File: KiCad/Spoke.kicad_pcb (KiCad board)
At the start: 2 copper layers, 50 x 100 mm, 128 parts, among them J1 B2B-PH-K-S, J10 BL-A, J11 BL-C, J12 Amphenol 132289, J2 BAT+, J3 BAT-, J4 GCT USB4105/USB4110, J5 CHG+, J6 CHG-, J7 PLS-1x3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

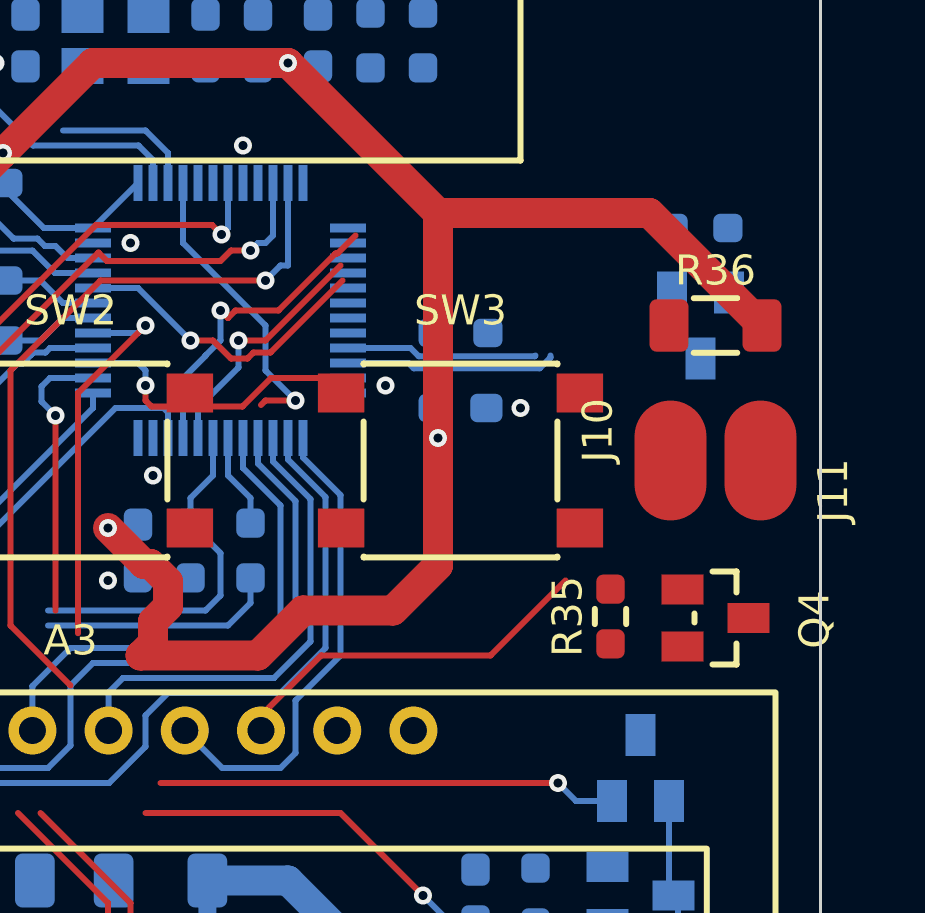
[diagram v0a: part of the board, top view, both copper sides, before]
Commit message: Route BL
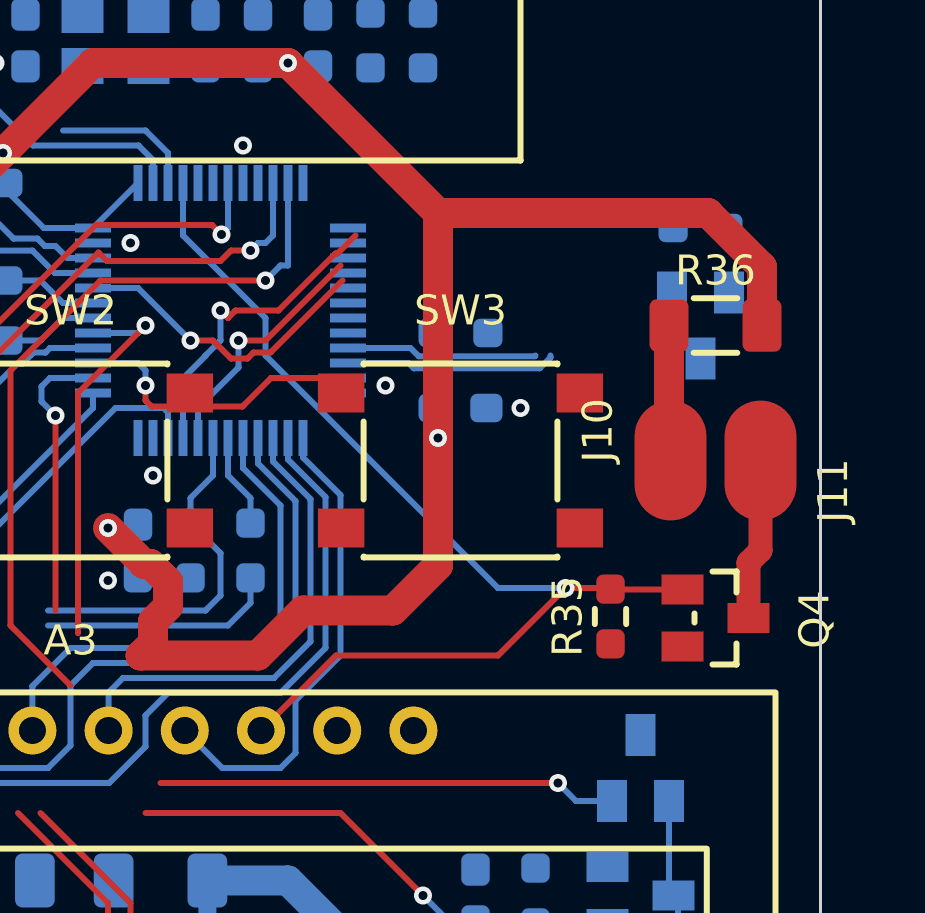
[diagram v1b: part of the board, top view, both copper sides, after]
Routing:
- net LCD_BL: track 22.0 -> 36.1 mm
- net Net-(Q4-D): track 0.00 -> 4.42 mm
- net Net-(J10-Pad1): track 0.00 -> 3.52 mm
- net +3V3: track 275.3 -> 276.4 mm
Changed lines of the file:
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@@
 	)
 	(segment
+		(start 121.25 91.75)
+		(end 123.05 93.55)
+		(width 1)
+		(layer "F.Cu")
+		(net 3)
+	)
+	(segment
 		(start 94.5 114)
 		(end 91.090214 114)
@@
 	)
 	(segment
-		(start 119.3 91.75)
-		(end 123.05 95.5)
-		(width 1)
-		(layer "F.Cu")
-		(net 3)
-	)
-	(segment
 		(start 84.25 72.75)
 		(end 84.75 73.25)
@@
 	)
 	(segment
+		(start 112.25 91.75)
+		(end 121.25 91.75)
+		(width 1)
+		(layer "F.Cu")
+		(net 3)
+	)
+	(segment
 		(start 89.199 113.6385)
 		(end 90.8625 111.975)
@@
 	)
 	(segment
+		(start 123.05 93.55)
+		(end 123.05 95.5)
+		(width 1)
+		(layer "F.Cu")
+		(net 3)
+	)
+	(segment
 		(start 91.5 87.017272)
 		(end 97.017272 81.5)
@@
 	)
 	(segment
-		(start 112.25 91.75)
-		(end 119.3 91.75)
-		(width 1)
-		(layer "F.Cu")
-		(net 3)
-	)
-	(segment
 		(start 88.75 54)
 		(end 102.5 54)
@@
 	)
 	(segment
-		(start 108.35 106.5)
-		(end 114 106.5)
+		(start 106.35 109)
+		(end 108.85 106.5)
 		(width 0.2)
 		(layer "F.Cu")
@@
 	)
 	(segment
-		(start 106.35 108.5)
-		(end 108.35 106.5)
+		(start 108.85 106.5)
+		(end 114.25 106.5)
 		(width 0.2)
 		(layer "F.Cu")
@@
 	)
 	(segment
-		(start 114 106.5)
-		(end 116.5 104)
+		(start 116.5 104.25)
+		(end 117.9625 104.25)
 		(width 0.2)
 		(layer "F.Cu")
@@
 	)
 	(segment
-		(start 106.5 98)
-		(end 106.35 98.15)
+		(start 118.0125 104.3)
+		(end 118 104.2875)
 		(width 0.2)
 		(layer "F.Cu")
@@
 	)
 	(segment
-		(start 107.5 98)
-		(end 106.5 98)
+		(start 114.25 106.5)
+		(end 116.5 104.25)
+		(width 0.2)
+		(layer "F.Cu")
+		(net 44)
+	)
+	(segment
+		(start 120.4 104.3)
+		(end 118.0125 104.3)
+		(width 0.2)
+		(layer "F.Cu")
+		(net 44)
+	)
+	(segment
+		(start 117.9625 104.25)
+		(end 118 104.2875)
 		(width 0.2)
 		(layer "F.Cu")
@@
 	)
 	(via
-		(at 107.5 98)
+		(at 116.5 104.25)
 		(size 0.6)
 		(drill 0.3)
@@
 	)
 	(segment
-		(start 106.5 95.5)
-		(end 103.75 92.75)
+		(start 103.75 92.5)
+		(end 106.5 95.25)
 		(width 0.2)
 		(layer "B.Cu")
@@
 	)
 	(segment
-		(start 107.5 98)
-		(end 106.5 97)
+		(start 114.25 104.25)
+		(end 116.5 104.25)
 		(width 0.2)
 		(layer "B.Cu")
@@
 	)
 	(segment
-		(start 103.75 92.75)
-		(end 103.75 90.75)
+		(start 106.5 96.5)
+		(end 114.25 104.25)
 		(width 0.2)
 		(layer "B.Cu")
@@
 	)
 	(segment
-		(start 106.5 97)
-		(end 106.5 95.5)
+		(start 106.5 95.25)
+		(end 106.5 96.5)
+		(width 0.2)
+		(layer "B.Cu")
+		(net 44)
+	)
+	(segment
+		(start 103.75 90.75)
+		(end 103.75 92.5)
 		(width 0.2)
 		(layer "B.Cu")
@@
 	)
 	(segment
+		(start 122.6 103.4)
+		(end 122.6 105.25)
+		(width 0.8)
+		(layer "F.Cu")
+		(net 83)
+	)
+	(segment
+		(start 123 103)
+		(end 122.6 103.4)
+		(width 0.8)
+		(layer "F.Cu")
+		(net 83)
+	)
+	(segment
+		(start 123 101)
+		(end 123 103)
+		(width 0.8)
+		(layer "F.Cu")
+		(net 83)
+	)
+	(segment
 		(start 99.75 117.05)
 		(end 98.8 118)
@@
 	)
 	(segment
+		(start 119.95 95.5)
+		(end 119.95 98.95)
+		(width 1)
+		(layer "F.Cu")
+		(net 90)
+	)
+	(segment
+		(start 119.95 98.95)
+		(end 120 99)
+		(width 1)
+		(layer "F.Cu")
+		(net 90)
+	)
+	(segment

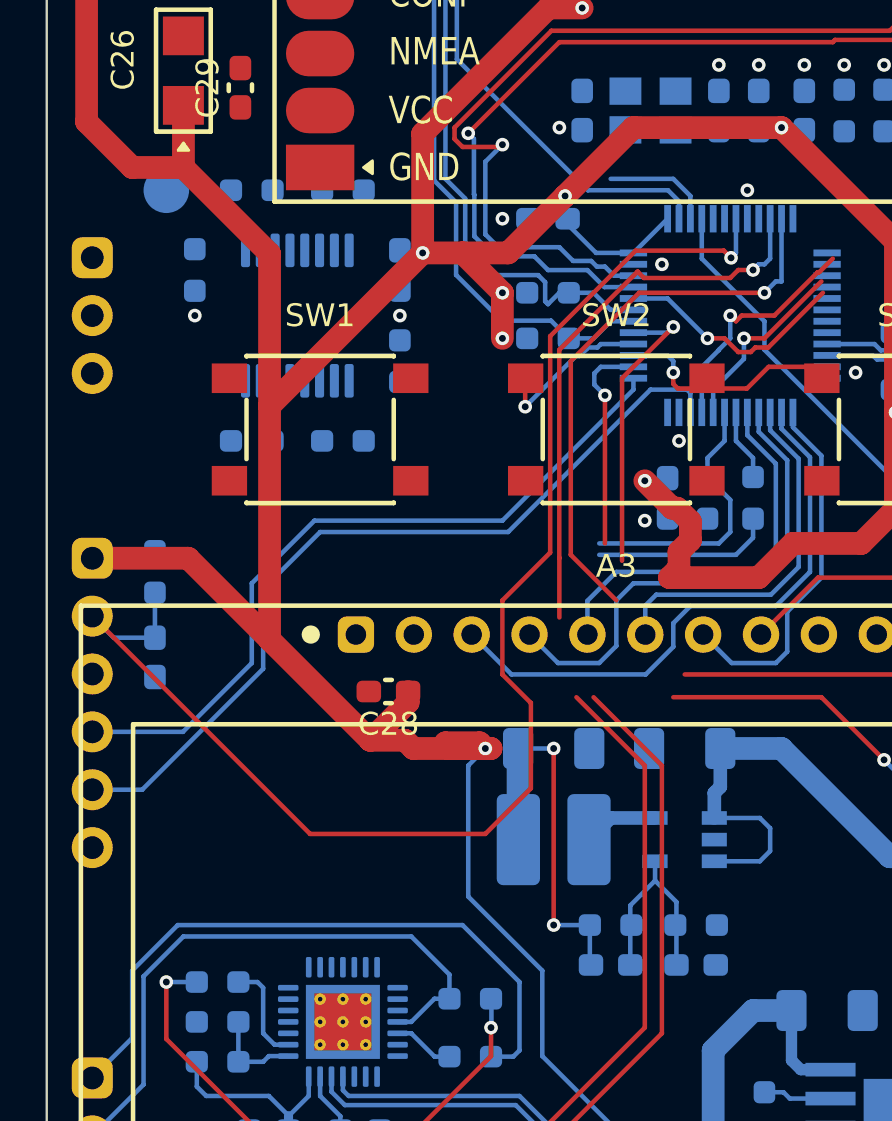
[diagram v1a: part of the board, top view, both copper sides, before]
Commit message: Route MUX #1
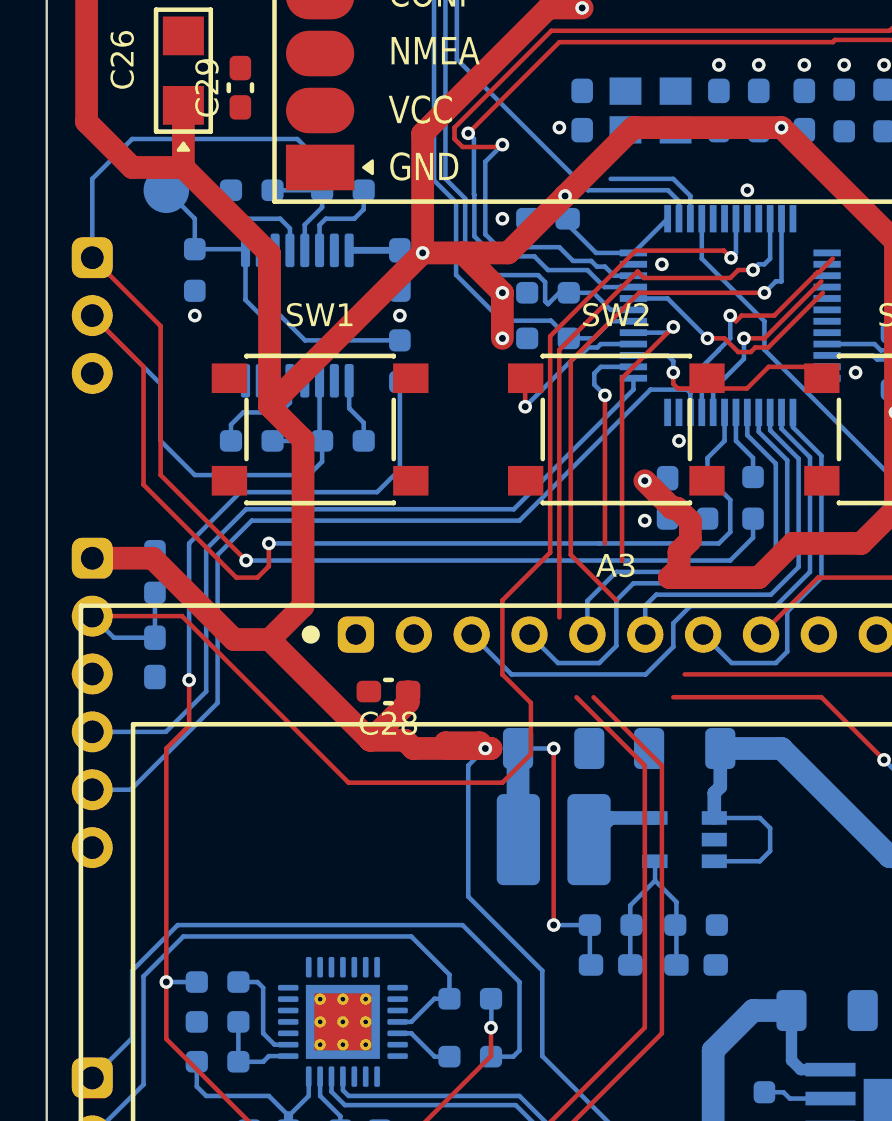
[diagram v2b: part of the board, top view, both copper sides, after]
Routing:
- net CONSOLE_TXD: track 7.90 -> 60.6 mm, vias 0 -> 1
- net CONSOLE_RXD: track 11.9 -> 63.7 mm, vias 0 -> 1
- net VDD: track 32.8 -> 66.9 mm, vias 3 -> 4
- net Net-(U5-S1): track 0.00 -> 11.6 mm
- net MUX_BLE_USB: track 4.81 -> 13.7 mm
- net BLE_RXD: track 0.00 -> 4.73 mm
- net USB_TXD: track 28.7 -> 33.3 mm
- net USB_RXD: track 26.5 -> 30.7 mm
- net +3V3: track 276.4 -> 279.9 mm
- net BLE_TXD: track 0.00 -> 2.90 mm
- net MCU_RESET: track 61.8 -> 59.1 mm
- net SWD_IO: track 36.5 -> 38.2 mm
- net SWD_CLK: track 32.5 -> 34.1 mm

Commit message: Route MUX #2
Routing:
- net USB_RXD: track 30.7 -> 85.4 mm, vias 0 -> 1
- net USB_TXD: track 33.3 -> 84.1 mm, vias 0 -> 1
- net BLE_RXD: track 4.73 -> 33.0 mm, vias 0 -> 2
- net BLE_TXD: track 2.90 -> 27.2 mm, vias 0 -> 2
- net +3V3: track 279.9 -> 281.2 mm
- net CONSOLE_TXD: track 60.6 -> 61.2 mm

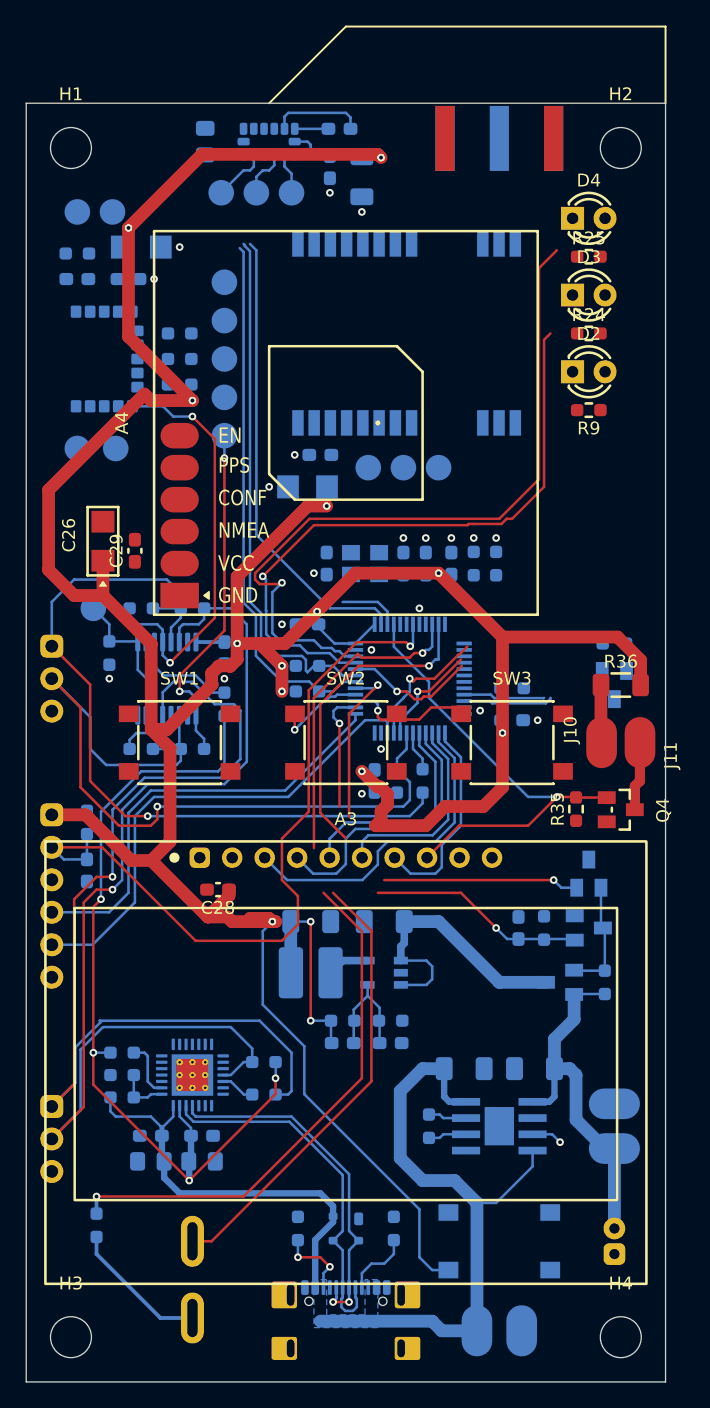
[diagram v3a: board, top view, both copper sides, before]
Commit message: Route buttons
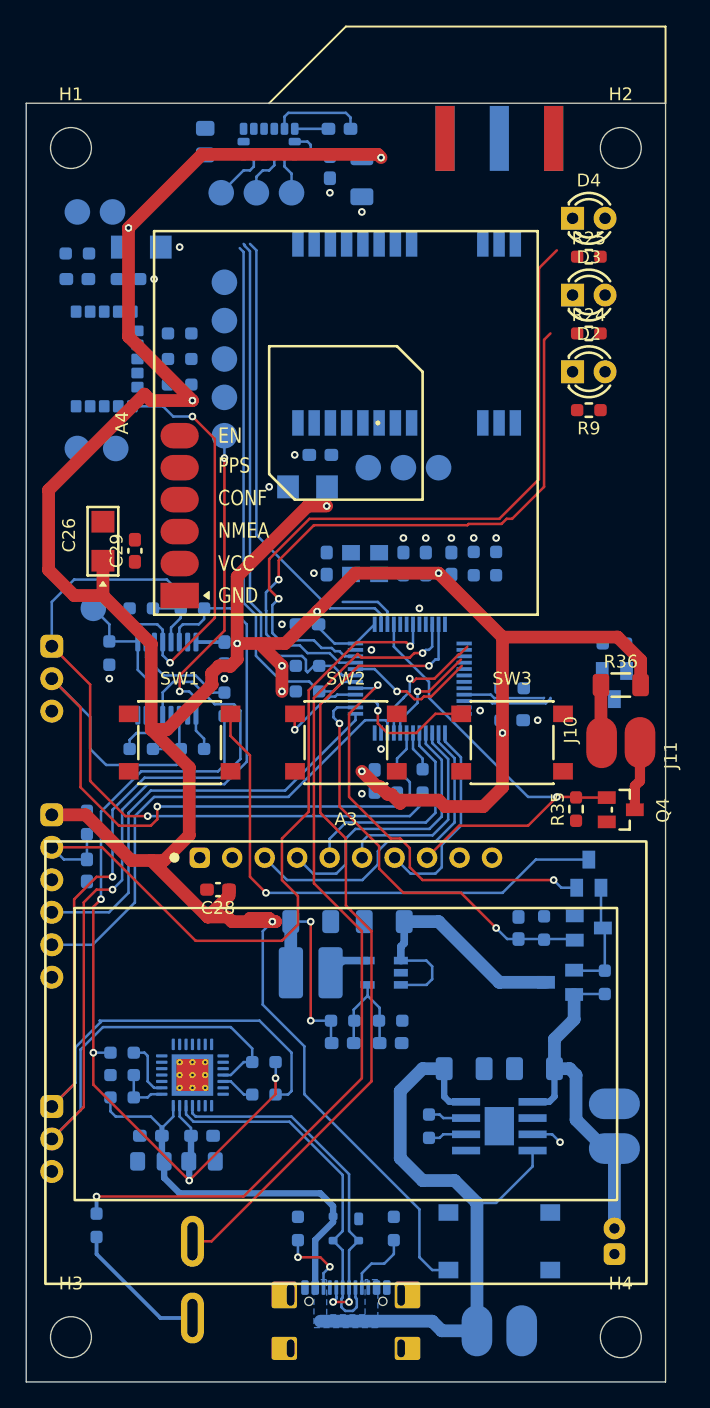
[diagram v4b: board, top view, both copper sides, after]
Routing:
- net Net-(D1-Pad3): track 0.00 -> 41.5 mm, vias 0 -> 1
- net PWR_HOLD: track 26.4 -> 33.2 mm
- net BTN_PWR: track 28.3 -> 33.2 mm
- net BUZZER_N: track 59.9 -> 63.8 mm
- net BUZZER_P: track 66.3 -> 70.1 mm
- net LED_GREEN: track 58.0 -> 55.7 mm
- net +3V3: track 281.2 -> 279.3 mm
- net BTN_ESC: track 9.85 -> 10.8 mm

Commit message: Route Lora
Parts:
- moved TP12 1.50 mm to (107.2, 80.0)
- moved TP14 1.50 mm to (104.5, 80.0)
- moved TP16 1.50 mm to (101.8, 80.0)
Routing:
- net RF_MISO: track 0.00 -> 46.9 mm
- net RF_BUSY: track 0.00 -> 45.6 mm, vias 0 -> 2
- net RF_IRQ: track 0.00 -> 44.9 mm, vias 0 -> 2
- net RF_MOSI: track 0.00 -> 41.4 mm
- net RF_SCK: track 0.00 -> 40.0 mm
- net RF_RESET: track 0.00 -> 39.4 mm, vias 0 -> 2
- net RF_CS: track 0.00 -> 38.3 mm
- net +3V3: track 279.3 -> 297.6 mm
- net MUX_BLE_USB: track 13.3 -> 29.1 mm, vias 0 -> 2
- net Net-(U6-PD0): track 0.00 -> 9.51 mm
- net RF_RXEN: track 10.5 -> 18.2 mm
- net VBAT_SENSE: track 0.00 -> 7.62 mm
- net Net-(U6-PD1): track 0.00 -> 6.70 mm
- net RF_TXEN: track 8.24 -> 14.6 mm
- net Net-(A2-DIO2): track 0.00 -> 5.70 mm
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
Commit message: Route Boot
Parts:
- moved R17 12.5 mm to (120.2, 104.8), turned to 180 degrees
- moved Q3 6.05 mm to (120.2, 101.5), turned to 180 degrees
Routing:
- net VBUS: track 84.5 -> 149.7 mm, vias 0 -> 3
- net Net-(D2-K): track 2.40 -> 67.1 mm, vias 1 -> 2
- net BOOT0: track 10.4 -> 65.2 mm, vias 1 -> 2
- net RF_TXEN: track 14.6 -> 36.7 mm, vias 1 -> 2
- net RF_RXEN: track 18.2 -> 37.7 mm, vias 1 -> 2
- net PPS_BOOT1: track 2.84 -> 20.2 mm, vias 0 -> 2
- net GPS_PPS: track 0.00 -> 14.1 mm
- net GPS_RXD: track 6.38 -> 19.3 mm
- net GPS_TXD: track 7.04 -> 19.7 mm
- net RF_MOSI: track 41.4 -> 42.5 mm
- net RF_SCK: track 40.0 -> 41.2 mm
- net RF_RESET: track 39.4 -> 40.6 mm
- net RF_MISO: track 46.9 -> 48.1 mm
- net RF_IRQ: track 44.9 -> 46.1 mm
- net RF_CS: track 38.3 -> 39.5 mm
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
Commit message: Route GPS
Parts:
- moved Q3 1.25 mm to (119.0, 101.5)
- moved R17 1.25 mm to (119.0, 104.8)
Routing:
- net GPS_TXD: track 19.7 -> 73.8 mm, vias 0 -> 1
- net VCC: track 22.5 -> 73.1 mm, vias 0 -> 2
- net GPS_RXD: track 19.3 -> 67.7 mm, vias 0 -> 1
- net GPS_PPS: track 14.1 -> 56.6 mm, vias 0 -> 1
- net +3V3: track 298.7 -> 307.8 mm
- net Net-(D4-A): track 0.00 -> 3.15 mm
- net Net-(D3-A): track 0.00 -> 3.15 mm
- net Net-(D2-A): track 0.00 -> 3.15 mm
- net BOOT0: track 65.2 -> 62.2 mm
- net PPS_BOOT1: track 20.2 -> 19.0 mm
- net LED_RED: track 49.4 -> 50.5 mm
- net (no net): vias 1 -> 0

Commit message: Route MCU
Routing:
- net +3V3: track 307.8 -> 313.7 mm
- net BUZZER_P: track 68.6 -> 66.8 mm
- net BUZZER_N: track 61.8 -> 60.1 mm
- net I2C_SDA: track 44.8 -> 45.6 mm
- net BTN_ESC: track 11.9 -> 11.1 mm
- net GPS_TXD: track 73.8 -> 74.5 mm
- net PWR_HOLD: track 33.2 -> 32.6 mm
